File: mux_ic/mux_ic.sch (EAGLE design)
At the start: 12 parts, among them U2 TEXAS_INSTRUMENTS_CD74HC4067M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, U5 TEXAS_INSTRUMENTS_CD74HC4067M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, U6 TEXAS_INSTRUMENTS_CD74HC4067M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, U7 TEXAS_INSTRUMENTS_CD74HC4067M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

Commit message: update to receive and send
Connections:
- removed net N$10: JP3.2, U7.COMMON_INPUT/OUTPUT
- net N$4: now also JP3.2; no longer JP2.1
- net N$5: now also JP2.1, U7.COMMON_INPUT/OUTPUT; no longer JP2.2
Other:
- moved on the sheet: JP2
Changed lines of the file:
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@@
 <part name="U7" library="Texas Instruments - CD74HC4067M96" deviceset="TEXAS_INSTRUMENTS_CD74HC4067M96" device="TEXAS_INSTRUMENTS_CD74HC4067M96_0_0"/>
 <part name="JP1" library="jumper" library_urn="urn:adsk.eagle:library:252" deviceset="JP2W" device="" package3d_urn="urn:adsk.eagle:package:15456/1"/>
-<part name="JP2" library="jumper" library_urn="urn:adsk.eagle:library:252" deviceset="JP1E" device="" package3d_urn="urn:adsk.eagle:package:15455/1"/>
 <part name="JP3" library="jumper" library_urn="urn:adsk.eagle:library:252" deviceset="JP1E" device="" package3d_urn="urn:adsk.eagle:package:15455/1"/>
 <part name="JP4" library="jumper" library_urn="urn:adsk.eagle:library:252" deviceset="JP4E" device="" package3d_urn="urn:adsk.eagle:package:15463/1"/>
@@
 <part name="JP7" library="jumper" library_urn="urn:adsk.eagle:library:252" deviceset="JP4E" device="" package3d_urn="urn:adsk.eagle:package:15463/1"/>
 <part name="JP8" library="jumper" library_urn="urn:adsk.eagle:library:252" deviceset="JP8Q" device="" package3d_urn="urn:adsk.eagle:package:15461/1"/>
+<part name="JP2" library="jumper" library_urn="urn:adsk.eagle:library:252" deviceset="JP1E" device="" package3d_urn="urn:adsk.eagle:package:15455/1"/>
 </parts>
 <sheets>
@@
 <attribute name="VALUE" x="13.335" y="177.8" size="1.778" layer="96" rot="R90"/>
 </instance>
-<instance part="JP2" gate="A" x="78.74" y="144.78" smashed="yes">
-<attribute name="NAME" x="77.47" y="144.78" size="1.778" layer="95" rot="R90"/>
-<attribute name="VALUE" x="84.455" y="144.78" size="1.778" layer="96" rot="R90"/>
-</instance>
 <instance part="JP3" gate="A" x="-139.7" y="215.9" smashed="yes">
 <attribute name="NAME" x="-140.97" y="215.9" size="1.778" layer="95" rot="R90"/>
@@
 <attribute name="NAME" x="-223.52" y="58.42" size="1.778" layer="95" rot="R180"/>
 <attribute name="VALUE" x="-223.52" y="83.185" size="1.778" layer="96" rot="R180"/>
+</instance>
+<instance part="JP2" gate="A" x="114.3" y="-15.24" smashed="yes">
+<attribute name="NAME" x="113.03" y="-15.24" size="1.778" layer="95" rot="R90"/>
+<attribute name="VALUE" x="120.015" y="-15.24" size="1.778" layer="96" rot="R90"/>
 </instance>
 </instances>
@@
 <pinref part="U5" gate="G$0" pin="COMMON_INPUT/OUTPUT"/>
 <wire x1="78.74" y1="96.52" x2="76.2" y2="96.52" width="0.1524" layer="91"/>
-<pinref part="JP2" gate="A" pin="1"/>
-<wire x1="78.74" y1="96.52" x2="78.74" y2="142.24" width="0.1524" layer="91"/>
+<wire x1="78.74" y1="96.52" x2="78.74" y2="121.92" width="0.1524" layer="91"/>
+<wire x1="78.74" y1="121.92" x2="22.86" y2="121.92" width="0.1524" layer="91"/>
+<wire x1="22.86" y1="121.92" x2="22.86" y2="200.66" width="0.1524" layer="91"/>
+<wire x1="22.86" y1="200.66" x2="-137.16" y2="200.66" width="0.1524" layer="91"/>
+<wire x1="-137.16" y1="200.66" x2="-137.16" y2="213.36" width="0.1524" layer="91"/>
+<pinref part="JP3" gate="A" pin="2"/>
 </segment>
 </net>
@@
 <pinref part="U6" gate="G$0" pin="COMMON_INPUT/OUTPUT"/>
 <wire x1="76.2" y1="5.08" x2="81.28" y2="5.08" width="0.1524" layer="91"/>
-<pinref part="JP2" gate="A" pin="2"/>
-<wire x1="81.28" y1="5.08" x2="81.28" y2="142.24" width="0.1524" layer="91"/>
-</segment>
-</net>
-<net name="N$10" class="0">
-<segment>
-<pinref part="JP3" gate="A" pin="2"/>
-<wire x1="-137.16" y1="213.36" x2="-137.16" y2="195.58" width="0.1524" layer="91"/>
-<wire x1="-137.16" y1="195.58" x2="-58.42" y2="195.58" width="0.1524" layer="91"/>
-<wire x1="-58.42" y1="195.58" x2="-58.42" y2="-66.04" width="0.1524" layer="91"/>
 <wire x1="-58.42" y1="-66.04" x2="-68.58" y2="-66.04" width="0.1524" layer="91"/>
 <pinref part="U7" gate="G$0" pin="COMMON_INPUT/OUTPUT"/>
 <wire x1="-68.58" y1="-66.04" x2="-68.58" y2="-58.42" width="0.1524" layer="91"/>
-</segment>
-</net>
+<wire x1="-58.42" y1="-66.04" x2="-58.42" y2="-93.98" width="0.1524" layer="91"/>
+<wire x1="-58.42" y1="-93.98" x2="114.3" y2="-93.98" width="0.1524" layer="91"/>
+<wire x1="116.84" y1="-93.98" x2="114.3" y2="-93.98" width="0.1524" layer="91"/>
+<wire x1="114.3" y1="-93.98" x2="114.3" y2="-25.4" width="0.1524" layer="91"/>
+<pinref part="JP2" gate="A" pin="1"/>
+<wire x1="114.3" y1="-25.4" x2="114.3" y2="-17.78" width="0.1524" layer="91"/>
+<wire x1="81.28" y1="5.08" x2="81.28" y2="-25.4" width="0.1524" layer="91"/>
+<wire x1="81.28" y1="-25.4" x2="114.3" y2="-25.4" width="0.1524" layer="91"/>
+<junction x="114.3" y="-25.4"/>
+</segment>
+</net>

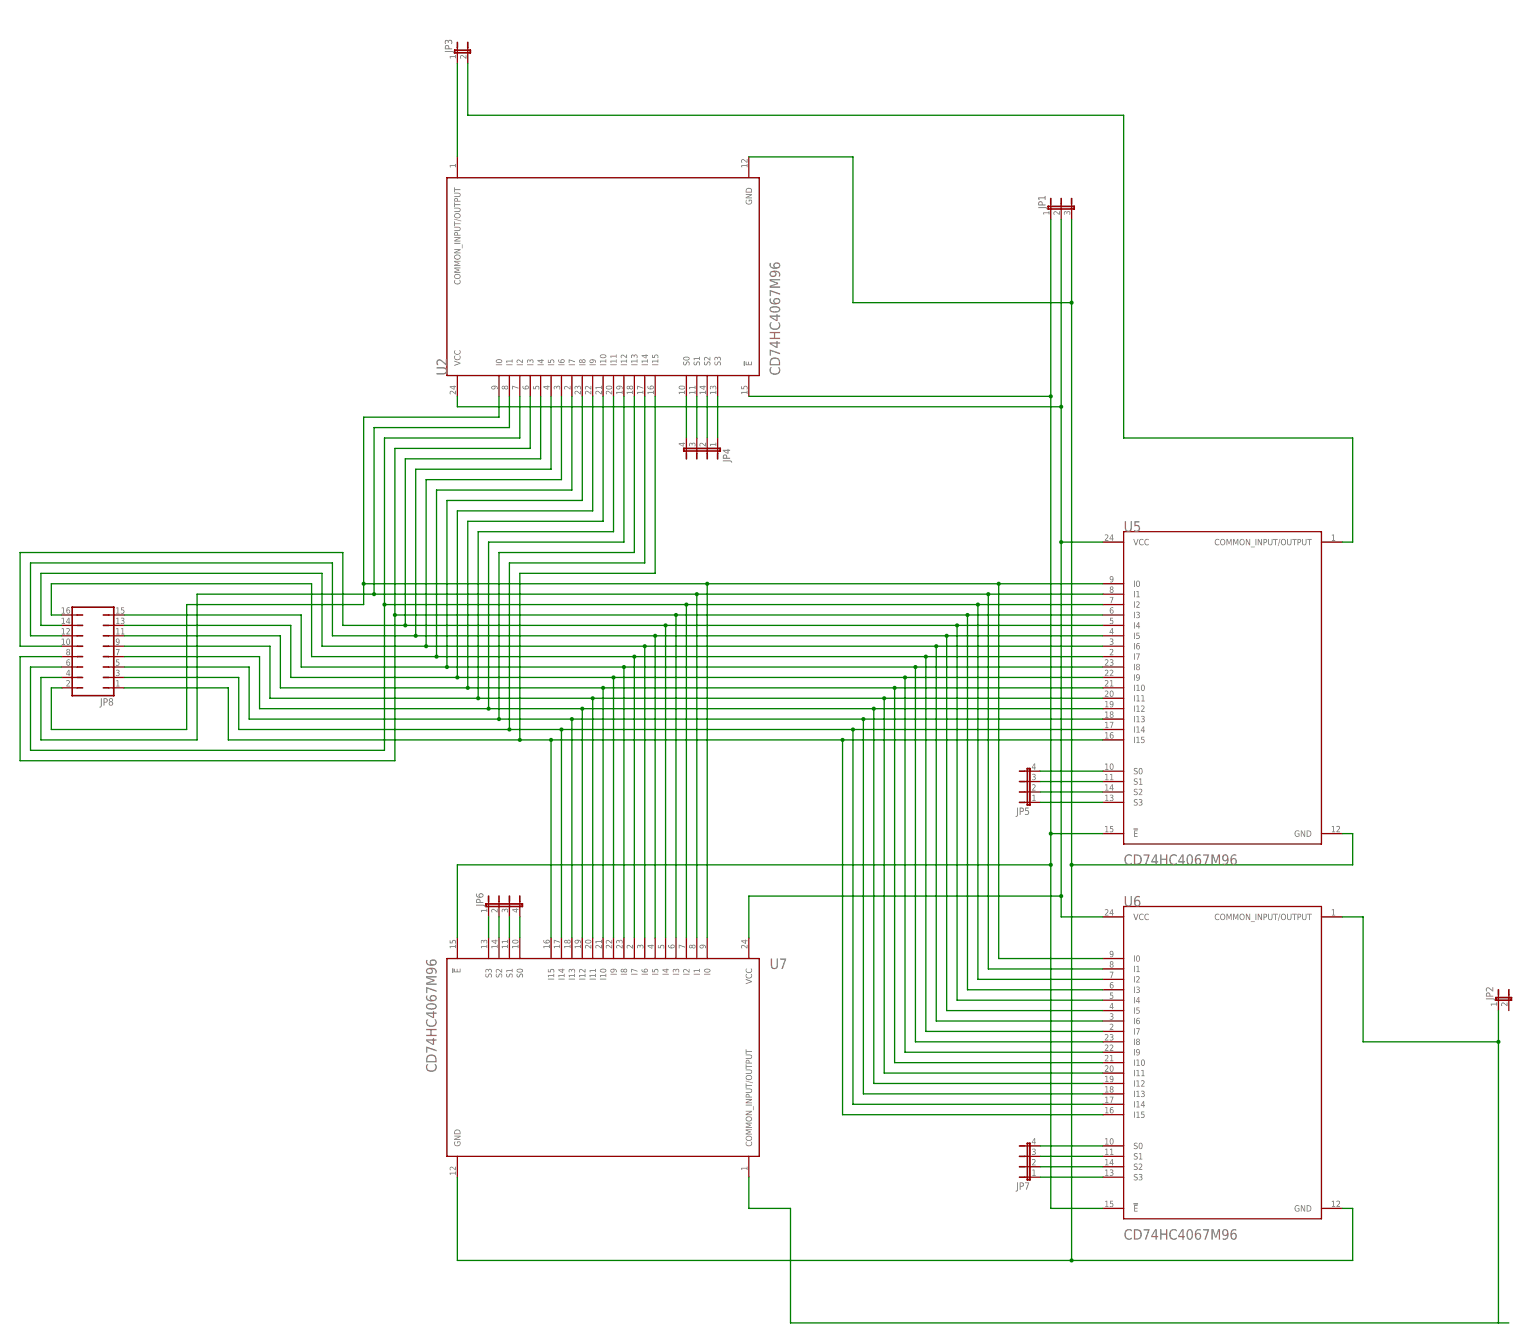
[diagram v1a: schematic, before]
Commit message: Gentrified board layout and component names
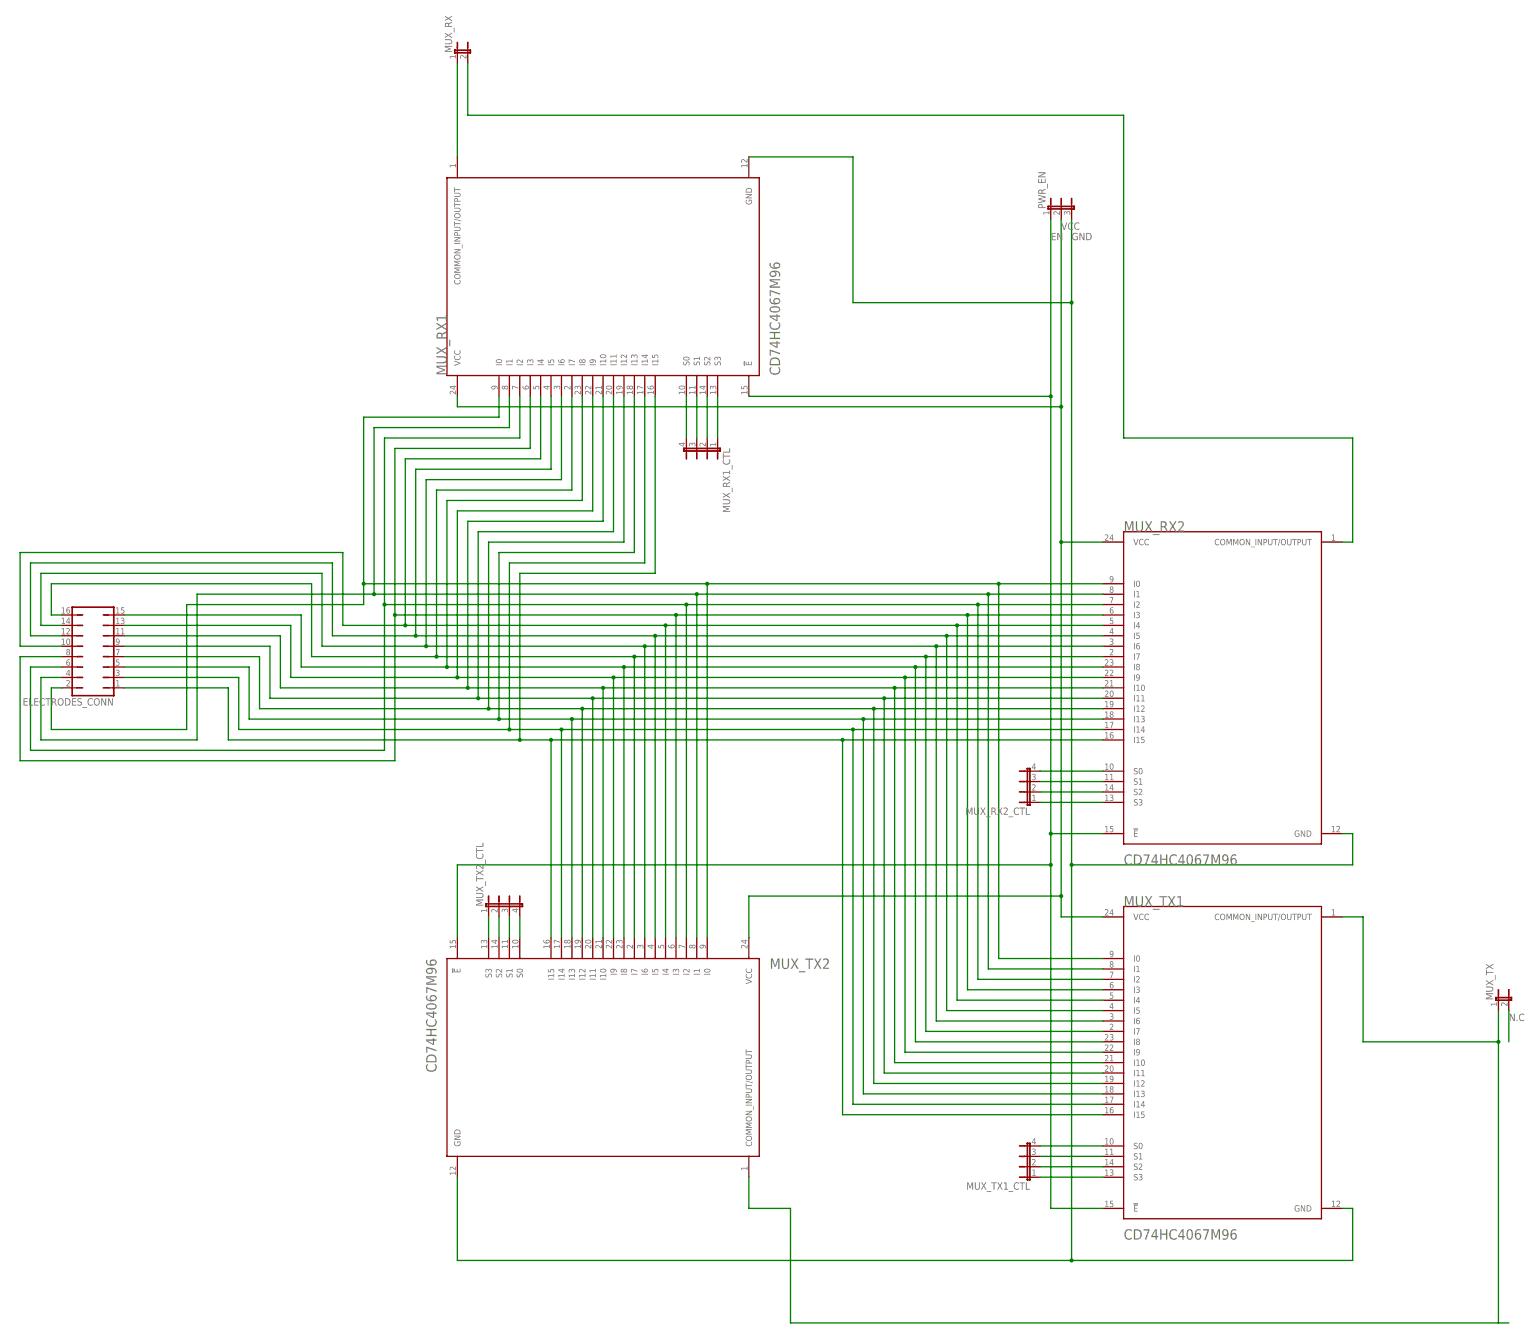
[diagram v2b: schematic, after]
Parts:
- renumbered JP1 to PWR_EN, JP2 to MUX_TX, JP3 to MUX_RX, JP4 to MUX_RX1_CTL, JP5 to MUX_RX2_CTL, JP6 to MUX_TX2_CTL, JP7 to MUX_TX1_CTL, JP8 to ELECTRODES_CONN, U2 to MUX_RX1, U5 to MUX_RX2, U6 to MUX_TX1, U7 to MUX_TX2
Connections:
- net N$7 renamed EN
- net N$8 renamed VCC
- net N$9 renamed GND
- new net N.C: MUX_TX.2
